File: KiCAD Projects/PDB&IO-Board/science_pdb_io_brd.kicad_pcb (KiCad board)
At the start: 2 copper layers, 148.6 x 94 mm, 61 parts, among them P1 PWR_IN, P10 MOTOR6_PWM, P11 ENCODER_1, P13 LIMIT1_IN, P14 LIMIT2_IN, P15 LIMIT3_IN, P16 ENCODER_3, P17 MOTOR1_PWM, P18 MOTOR2_PWM, P19 MOTOR3_PWM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

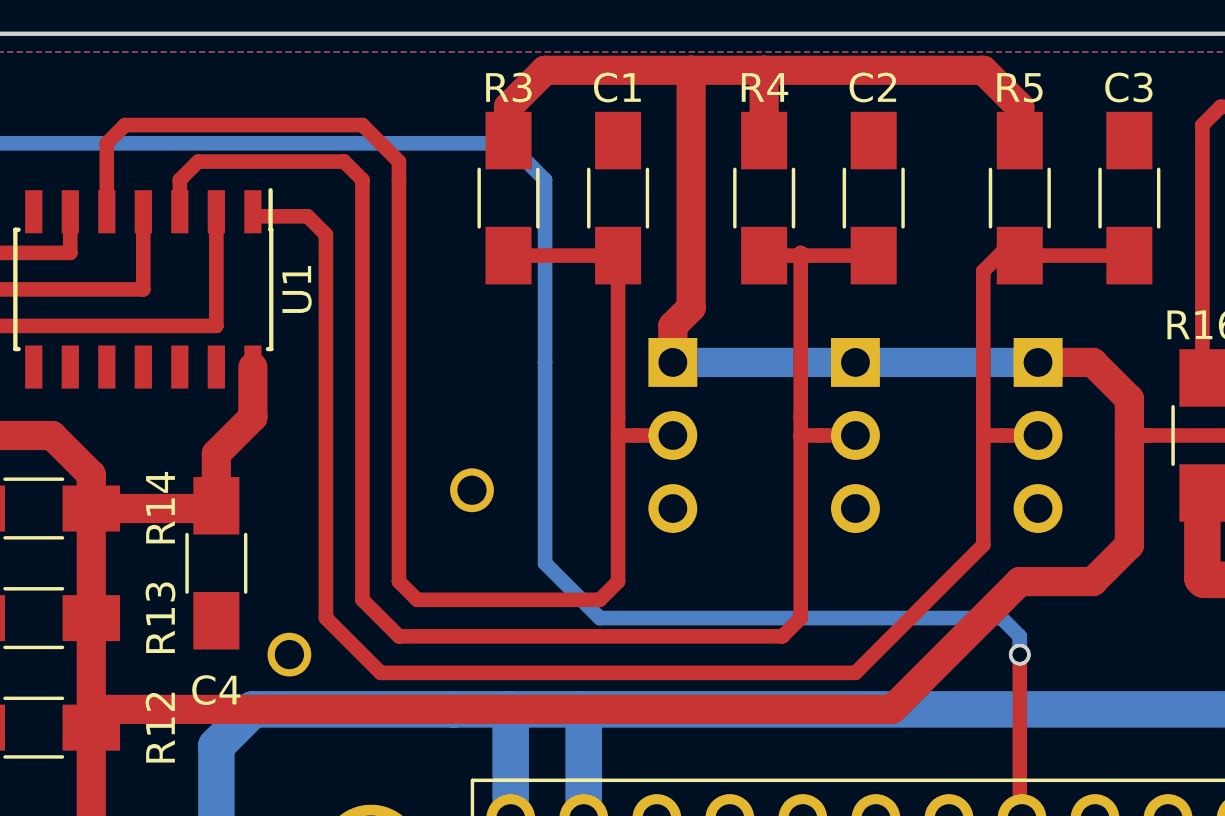
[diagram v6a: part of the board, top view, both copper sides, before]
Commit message: Finished Editing Connectors
Increased spacing for Molex connectors.
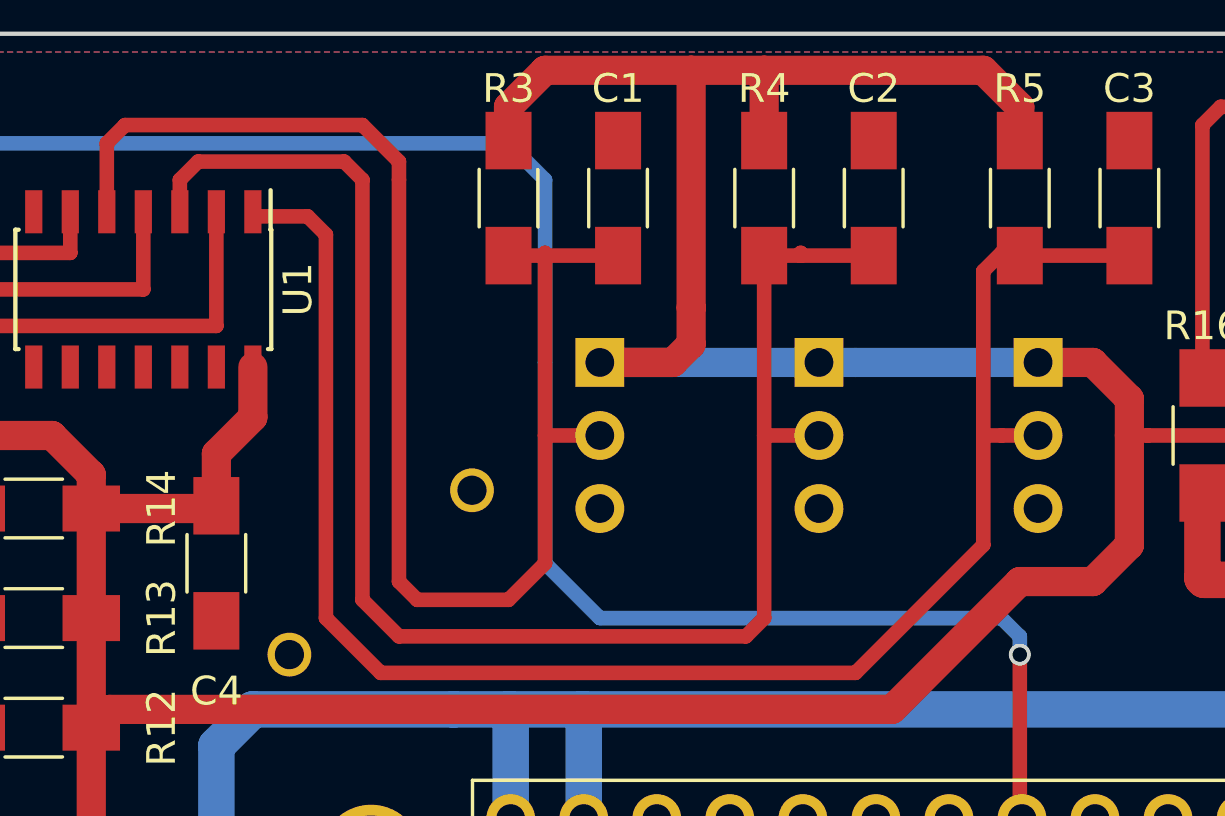
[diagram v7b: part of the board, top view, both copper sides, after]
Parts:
- moved P15 2.54 mm to (128.9, 33.0)
- moved P14 1.27 mm to (136.5, 33.0)
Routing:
- net +3V3: track 399.8 -> 404.9 mm
- net /B_LIM3: track 54.0 -> 50.6 mm
- net /B_LIM2: track 57.1 -> 56.5 mm
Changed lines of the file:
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@@
     (thickness 1.6)
     (drawings 95)
-    (tracks 485)
+    (tracks 486)
     (zones 0)
     (modules 61)
@@
   )
   (module Pin_Headers:Pin_Header_Straight_1x03_Pitch2.54mm (layer B.Cu)
-    (at 137.795 33.02 180)
+    (at 136.525 33.02 180)
     (descr "Through hole straight pin header, 1x03, 2.54mm pitch, single row")
     (tags "Through hole pin header THT 1x03 2.54mm single row")
@@
   )
   (module Pin_Headers:Pin_Header_Straight_1x03_Pitch2.54mm (layer B.Cu)
-    (at 131.445 33.02 180)
+    (at 128.905 33.02 180)
     (descr "Through hole straight pin header, 1x03, 2.54mm pitch, single row")
     (tags "Through hole pin header THT 1x03 2.54mm single row")
@@
     (effects (font (size 1.5 1.5) (thickness 0.3)) (justify mirror))
   )
-  (gr_text GND (at 128.27 38.1) (layer B.SilkS)
-    (effects (font (size 1 1) (thickness 0.15)) (justify left mirror))
-  )
-  (gr_text SW_IN (at 128.27 35.56) (layer B.SilkS)
-    (effects (font (size 1 1) (thickness 0.15)) (justify left mirror))
-  )
-  (gr_text 3.3V (at 128.27 33.02) (layer B.SilkS)
+  (gr_text GND (at 151.765 38.1) (layer B.SilkS)
+    (effects (font (size 1 1) (thickness 0.15)) (justify left mirror))
+  )
+  (gr_text SW_IN (at 153.035 35.56) (layer B.SilkS)
+    (effects (font (size 1 1) (thickness 0.15)) (justify left mirror))
+  )
+  (gr_text 3.3V (at 151.765 33.02) (layer B.SilkS)
     (effects (font (size 1 1) (thickness 0.15)) (justify left mirror))
   )
@@
     (effects (font (size 1 1) (thickness 0.15)) (justify left mirror))
   )
-  (gr_text "LIM 3" (at 131.445 42.545) (layer B.SilkS)
+  (gr_text "LIM 3" (at 128.905 42.545) (layer B.SilkS)
     (effects (font (size 1 1) (thickness 0.15)) (justify mirror))
   )
-  (gr_text "LIM 2" (at 137.795 42.545) (layer B.SilkS)
+  (gr_text "LIM 2" (at 136.525 42.545) (layer B.SilkS)
     (effects (font (size 1 1) (thickness 0.15)) (justify mirror))
   )
@@
   (segment (start 150.495 24.13) (end 153.035 24.13) (width 0.508) (layer F.Cu) (net 61))
   (segment (start 149.86 24.765) (end 150.495 24.13) (width 0.508) (layer F.Cu) (net 61))
-  (segment (start 129.54 35.56) (end 129.54 40.64) (width 0.508) (layer F.Cu) (net 69))
+  (segment (start 127 35.56) (end 127 40.005) (width 0.508) (layer F.Cu) (net 69))
+  (segment (start 122.555 41.275) (end 121.92 40.64) (width 0.508) (layer F.Cu) (net 69))
+  (segment (start 121.92 40.64) (end 121.92 26.67) (width 0.508) (layer F.Cu) (net 69))
+  (segment (start 121.92 26.67) (end 121.92 26.035) (width 0.508) (layer F.Cu) (net 69))
+  (segment (start 121.92 26.035) (end 120.65 24.765) (width 0.508) (layer F.Cu) (net 69))
+  (segment (start 120.65 24.765) (end 112.395 24.765) (width 0.508) (layer F.Cu) (net 69))
+  (segment (start 112.395 24.765) (end 111.76 25.4) (width 0.508) (layer F.Cu) (net 69))
   (segment (start 111.76 25.4) (end 111.76 27.78) (width 0.508) (layer F.Cu) (net 69))
-  (segment (start 112.395 24.765) (end 111.76 25.4) (width 0.508) (layer F.Cu) (net 69))
-  (segment (start 120.65 24.765) (end 112.395 24.765) (width 0.508) (layer F.Cu) (net 69))
-  (segment (start 121.92 26.035) (end 120.65 24.765) (width 0.508) (layer F.Cu) (net 69))
-  (segment (start 121.92 26.67) (end 121.92 26.035) (width 0.508) (layer F.Cu) (net 69))
-  (segment (start 121.92 40.64) (end 121.92 26.67) (width 0.508) (layer F.Cu) (net 69))
-  (segment (start 122.555 41.275) (end 121.92 40.64) (width 0.508) (layer F.Cu) (net 69))
-  (segment (start 128.905 41.275) (end 122.555 41.275) (width 0.508) (layer F.Cu) (net 69))
-  (segment (start 129.54 40.64) (end 128.905 41.275) (width 0.508) (layer F.Cu) (net 69))
-  (segment (start 130.175 35.56) (end 129.54 35.56) (width 0.508) (layer F.Cu) (net 69))
-  (segment (start 129.54 35.56) (end 129.54 34.925) (width 0.508) (layer F.Cu) (net 69))
-  (segment (start 129.54 29.305) (end 125.73 29.305) (width 0.508) (layer F.Cu) (net 69))
-  (segment (start 131.445 35.56) (end 130.175 35.56) (width 0.508) (layer F.Cu) (net 69))
-  (segment (start 129.54 34.925) (end 129.54 29.305) (width 0.508) (layer F.Cu) (net 69))
+  (segment (start 125.73 41.275) (end 122.555 41.275) (width 0.508) (layer F.Cu) (net 69))
+  (segment (start 127 40.005) (end 125.73 41.275) (width 0.508) (layer F.Cu) (net 69))
+  (segment (start 128.905 35.56) (end 127 35.56) (width 0.508) (layer F.Cu) (net 69))
+  (segment (start 127 35.56) (end 127 29.305) (width 0.508) (layer F.Cu) (net 69))
+  (segment (start 127 29.305) (end 127 29.21) (width 0.508) (layer F.Cu) (net 69))
+  (segment (start 127 29.21) (end 127 29.305) (width 0.508) (layer F.Cu) (net 69))
+  (segment (start 129.54 29.305) (end 127 29.305) (width 0.508) (layer F.Cu) (net 69))
+  (segment (start 127 29.305) (end 125.73 29.305) (width 0.508) (layer F.Cu) (net 69))
   (segment (start 129.54 29.305) (end 129.54 29.21) (width 0.508) (layer F.Cu) (net 69))
   (segment (start 129.54 29.21) (end 129.54 29.305) (width 0.508) (layer F.Cu) (net 69))
-  (segment (start 131.445 35.56) (end 130.81 35.56) (width 0.508) (layer B.Cu) (net 69))
-  (segment (start 135.89 35.56) (end 135.89 41.91) (width 0.508) (layer F.Cu) (net 70))
-  (segment (start 114.3 26.67) (end 114.3 27.78) (width 0.508) (layer F.Cu) (net 70))
+  (segment (start 134.62 35.56) (end 134.62 29.305) (width 0.508) (layer F.Cu) (net 70))
+  (segment (start 121.92 42.545) (end 133.985 42.545) (width 0.508) (layer F.Cu) (net 70))
+  (segment (start 121.92 42.545) (end 120.65 41.275) (width 0.508) (layer F.Cu) (net 70))
+  (segment (start 120.65 41.275) (end 120.65 26.67) (width 0.508) (layer F.Cu) (net 70))
+  (segment (start 120.65 26.67) (end 120.015 26.035) (width 0.508) (layer F.Cu) (net 70))
+  (segment (start 120.015 26.035) (end 114.935 26.035) (width 0.508) (layer F.Cu) (net 70))
   (segment (start 114.935 26.035) (end 114.3 26.67) (width 0.508) (layer F.Cu) (net 70))
-  (segment (start 120.015 26.035) (end 114.935 26.035) (width 0.508) (layer F.Cu) (net 70))
-  (segment (start 120.65 26.67) (end 120.015 26.035) (width 0.508) (layer F.Cu) (net 70))
-  (segment (start 120.65 41.275) (end 120.65 26.67) (width 0.508) (layer F.Cu) (net 70))
-  (segment (start 121.92 42.545) (end 120.65 41.275) (width 0.508) (layer F.Cu) (net 70))
-  (segment (start 135.255 42.545) (end 121.92 42.545) (width 0.508) (layer F.Cu) (net 70))
-  (segment (start 135.89 41.91) (end 135.255 42.545) (width 0.508) (layer F.Cu) (net 70))
+  (segment (start 114.3 27.78) (end 114.3 26.67) (width 0.508) (layer F.Cu) (net 70))
+  (segment (start 134.62 35.56) (end 136.525 35.56) (width 0.508) (layer F.Cu) (net 70))
+  (segment (start 134.62 41.91) (end 134.62 35.56) (width 0.508) (layer F.Cu) (net 70))
+  (segment (start 133.985 42.545) (end 134.62 41.91) (width 0.508) (layer F.Cu) (net 70))
   (segment (start 136.525 35.56) (end 135.89 35.56) (width 0.508) (layer F.Cu) (net 70))
-  (segment (start 135.89 29.305) (end 135.89 34.925) (width 0.508) (layer F.Cu) (net 70))
-  (segment (start 136.525 35.56) (end 137.795 35.56) (width 0.508) (layer F.Cu) (net 70))
-  (segment (start 135.89 35.56) (end 135.89 34.925) (width 0.508) (layer F.Cu) (net 70))
   (segment (start 135.89 29.305) (end 135.89 29.21) (width 0.508) (layer F.Cu) (net 70))
   (segment (start 135.89 29.21) (end 135.89 29.305) (width 0.508) (layer F.Cu) (net 70))
@@
   (segment (start 142.24 35.56) (end 142.875 35.56) (width 0.508) (layer F.Cu) (net 71))
   (segment (start 142.875 35.56) (end 144.145 35.56) (width 0.508) (layer F.Cu) (net 71))
+  (segment (start 136.525 33.02) (end 137.795 33.02) (width 1.016) (layer B.Cu) (net 72))
+  (segment (start 137.795 33.02) (end 144.145 33.02) (width 1.016) (layer B.Cu) (net 72))
+  (segment (start 136.525 33.02) (end 128.905 33.02) (width 1.016) (layer B.Cu) (net 72))
+  (segment (start 132.08 31.115) (end 132.08 32.385) (width 1.016) (layer F.Cu) (net 72))
+  (segment (start 132.08 22.86) (end 132.08 31.115) (width 1.016) (layer F.Cu) (net 72))
+  (segment (start 131.445 33.02) (end 128.905 33.02) (width 1.016) (layer F.Cu) (net 72))
+  (segment (start 132.08 32.385) (end 131.445 33.02) (width 1.016) (layer F.Cu) (net 72))
   (segment (start 111.22 83.725) (end 111.22 101.6) (width 1.016) (layer F.Cu) (net 72))
   (segment (start 111.22 81.28) (end 111.22 83.725) (width 1.016) (layer F.Cu) (net 72))
@@
   (segment (start 137.16 106.045) (end 137.16 109.22) (width 1.016) (layer F.Cu) (net 72))
   (segment (start 116.84 106.045) (end 116.84 109.22) (width 1.016) (layer F.Cu) (net 72))
-  (segment (start 132.08 22.86) (end 132.08 31.115) (width 1.016) (layer F.Cu) (net 72))
-  (segment (start 131.445 31.75) (end 131.445 33.02) (width 1.016) (layer F.Cu) (net 72))
-  (segment (start 132.08 31.115) (end 131.445 31.75) (width 1.016) (layer F.Cu) (net 72))
   (segment (start 134.62 22.86) (end 142.24 22.86) (width 1.016) (layer F.Cu) (net 72))
   (segment (start 143.51 24.13) (end 143.51 25.305) (width 1.016) (layer F.Cu) (net 72))
@@
   (segment (start 132.08 22.86) (end 134.62 22.86) (width 1.016) (layer F.Cu) (net 72))
   (segment (start 125.73 24.13) (end 125.73 25.305) (width 1.016) (layer F.Cu) (net 72))
-  (segment (start 144.145 33.02) (end 137.795 33.02) (width 1.016) (layer B.Cu) (net 72))
-  (segment (start 137.795 33.02) (end 131.445 33.02) (width 1.016) (layer B.Cu) (net 72))
   (segment (start 111.22 38.1) (end 111.22 36.925) (width 1.016) (layer F.Cu) (net 72))
   (segment (start 109.855 35.56) (end 102.87 35.56) (width 1.016) (layer F.Cu) (net 72))

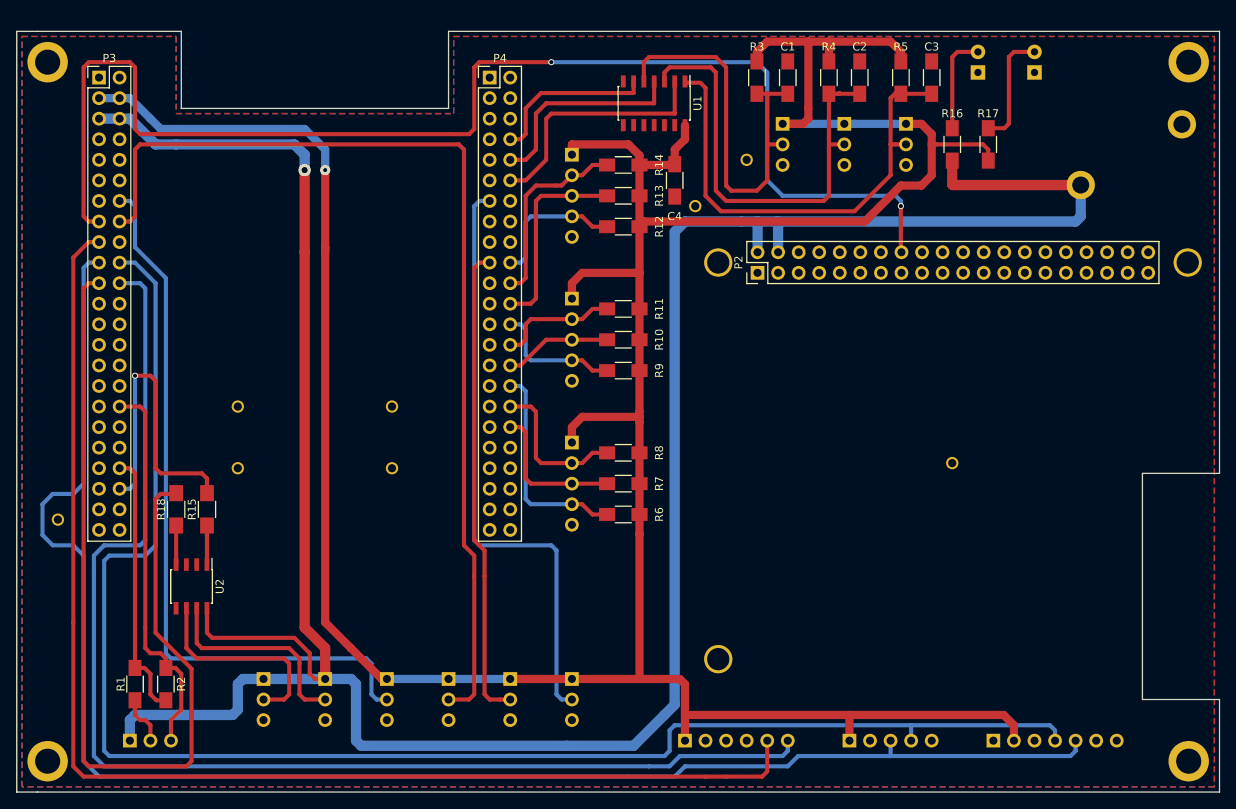
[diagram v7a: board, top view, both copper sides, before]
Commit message: Minor Updates
Changed capacitors to resistors (all 1206 Rs were 1206 Cs). Small
silkscreen changes.
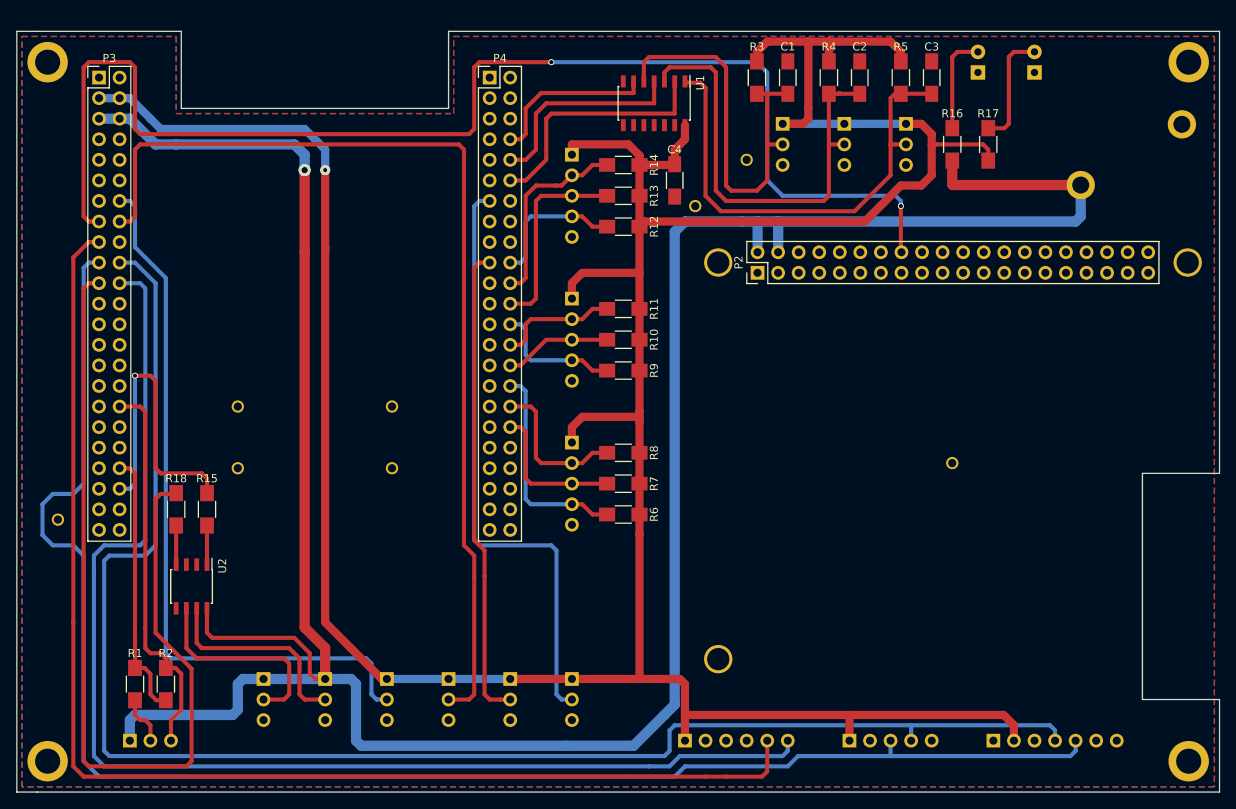
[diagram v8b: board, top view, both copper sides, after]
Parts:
- R1, R10, R11, R12, R13, R14, R16, R17, R2, R3, R4, R5, R6, R7, R8, R9: footprint Capacitors_SMD:C_1206_HandSoldering -> Resistors_SMD:R_1206_HandSoldering
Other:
- board text added: "Cutout for Beaglebone Ethernet connector"
- board text added: "Cutout for Raspberry Pi Ethernet connector"
- board text added: "MOTORS: 3.3V"
- board text added: "SERVOS: 5V"
- board text added: "V+"
